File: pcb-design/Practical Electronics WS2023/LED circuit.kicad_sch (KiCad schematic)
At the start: 0 parts

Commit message: Update voltage regulator
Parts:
- added D10, D11, D12, D13, D14, D15, D16, D17, D3, D4, D5, D6, D7, D8, D9: WS2812B, LED_SMD:LED_WS2812B_PLCC4_5.0x5.0mm_P3.2mm, symbol LED:WS2812B
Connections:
- new net: D15.2 (DOUT), D16.4 (DIN)
- new net: D14.2 (DOUT), D15.4 (DIN)
- new net: D11.2 (DOUT), D12.4 (DIN)
- new net: D4.2 (DOUT), D5.4 (DIN)
- new net: D3.2 (DOUT), D4.4 (DIN)
- new net: D10.2 (DOUT), D11.4 (DIN)
- new net: D10.4 (DIN), D9.2 (DOUT)
- new net: D8.2 (DOUT), D9.4 (DIN)
- new net: D16.2 (DOUT), D17.4 (DIN)
- new net: D13.2 (DOUT), D14.4 (DIN)
- new net: D6.2 (DOUT), D7.4 (DIN)
- new net: D5.2 (DOUT), D6.4 (DIN)
- new net +5V: D10.1 (VDD), D11.1 (VDD), D12.1 (VDD), D13.1 (VDD), D14.1 (VDD), D15.1 (VDD), D16.1 (VDD), D17.1 (VDD), D3.1 (VDD), D4.1 (VDD), D5.1 (VDD), D6.1 (VDD), D7.1 (VDD), D8.1 (VDD), D9.1 (VDD)
- new net GND: D10.3 (VSS), D11.3 (VSS), D12.3 (VSS), D13.3 (VSS), D14.3 (VSS), D15.3 (VSS), D16.3 (VSS), D17.3 (VSS), D3.3 (VSS), D4.3 (VSS), D5.3 (VSS), D6.3 (VSS), D7.3 (VSS), D8.3 (VSS), D9.3 (VSS)
- new net LED_ON_BOARD: D3.4 (DIN)
- new net R1_DOUT: D7.2 (DOUT), D8.4 (DIN)
- new net R2_DOUT: D12.2 (DOUT), D13.4 (DIN)
- no-connect marks 0 -> 1
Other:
- note added: "Onboard LED matrix"

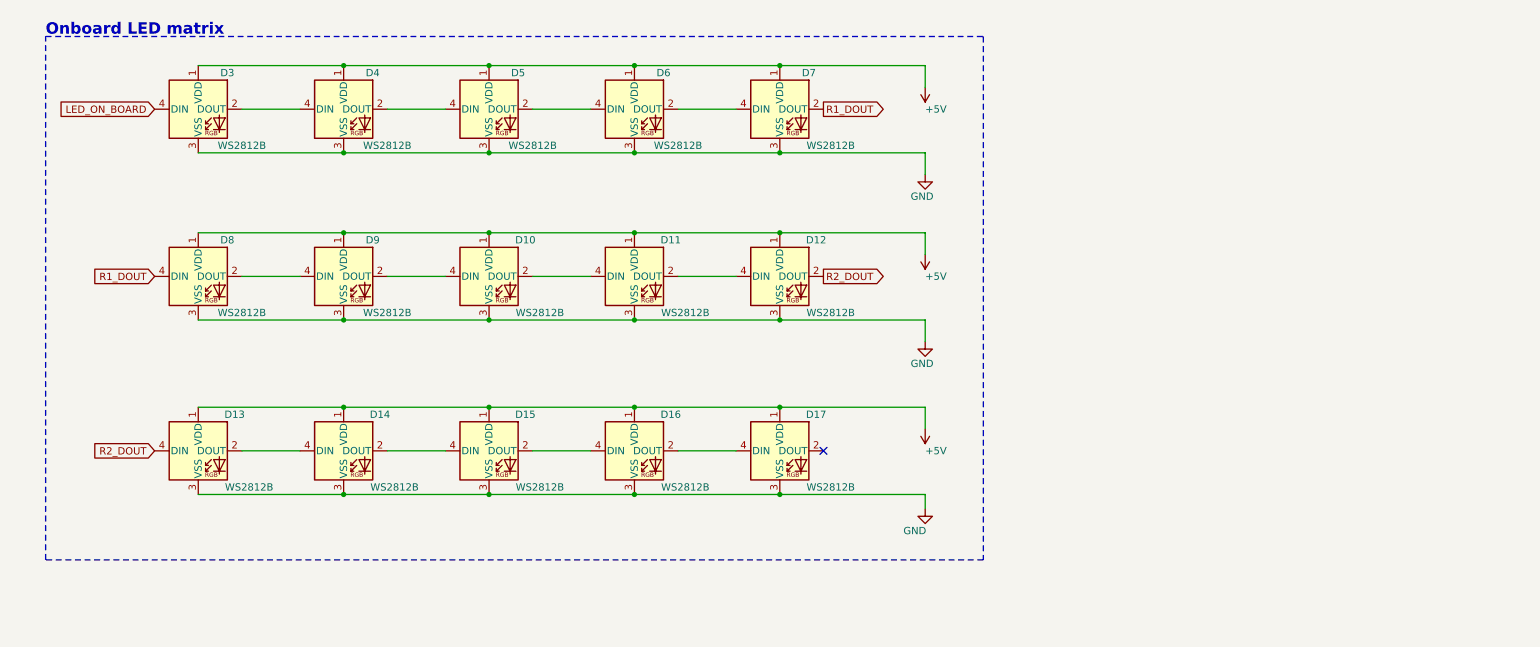
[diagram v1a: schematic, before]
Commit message: Power switch, logic switches, LED strip detection, onboard LEDs are 2x8.
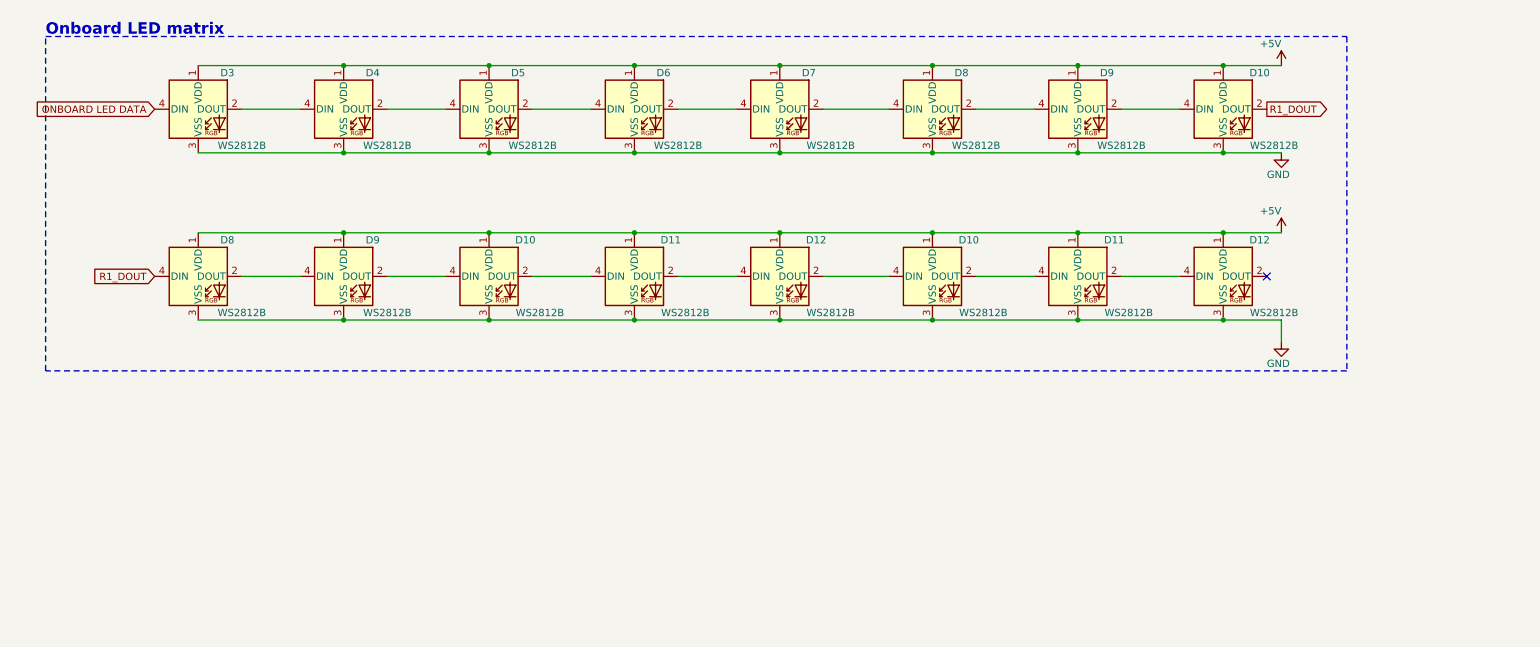
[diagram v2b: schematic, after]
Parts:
- removed D13, D14, D15, D16, D17: WS2812B, LED_SMD:LED_WS2812B_PLCC4_5.0x5.0mm_P3.2mm, symbol LED:WS2812B
- added D10 (x2), D11, D12, D8, D9: WS2812B, LED_SMD:LED_WS2812B_PLCC4_5.0x5.0mm_P3.2mm, symbol LED:WS2812B
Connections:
- net +5V: now also D10.1 (VDD), D10.1 (VDD), D11.1 (VDD), D12.1 (VDD), D8.1 (VDD), D9.1 (VDD)
- net GND: now also D10.3 (VSS), D10.3 (VSS), D11.3 (VSS), D12.3 (VSS), D8.3 (VSS), D9.3 (VSS)
- net R1_DOUT: now also D10.2 (DOUT); no longer D7.2 (DOUT)
- net LED_ON_BOARD renamed ONBOARD LED DATA
- net R2_DOUT: no longer names the net of D12.2 (DOUT)
- net R2_DOUT: now also D10.4 (DIN)
- new net: D8.2 (DOUT), D9.4 (DIN)
- new net: D7.2 (DOUT), D8.4 (DIN)
- new net: D10.4 (DIN), D9.2 (DOUT)
- new net: D11.2 (DOUT), D12.4 (DIN)
- new net: D10.2 (DOUT), D11.4 (DIN)

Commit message: Update schematic
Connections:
- net +5V renamed +12V

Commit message: Update schematic
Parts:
- removed D10 (x2), D11 (x2), D12 (x2): WS2812B, LED_SMD:LED_WS2812B_PLCC4_5.0x5.0mm_P3.2mm, symbol LED:WS2812B
- added C10, C11, C12, C13, C14, C15, C16, C17, C18, C19, C20, C21, C22, C23, C24, C25: 0.1uF, symbol Device:C
- added D10, D3, D4, D5, D6, D7: WS2812B, LED_SMD:LED_WS2812B_PLCC4_5.0x5.0mm_P3.2mm, symbol LED:WS2812B
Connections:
- net +12V: now also C10.1, C11.1, C12.1, C13.1, C14.1, C15.1, C16.1, C17.1, C18.1, C19.1, C20.1, C21.1, C22.1, C23.1, C24.1, C25.1, D10.1 (VDD), D3.1 (VDD), D4.1 (VDD), D5.1 (VDD), D6.1 (VDD), D7.1 (VDD)
- net GND: now also C10.2, C11.2, C12.2, C13.2, C14.2, C15.2, C16.2, C17.2, C18.2, C19.2, C20.2, C21.2, C22.2, C23.2, C24.2, C25.2, D10.3 (VSS), D3.3 (VSS), D4.3 (VSS), D5.3 (VSS), D6.3 (VSS), D7.3 (VSS)
- net R1_DOUT: now also D3.4 (DIN); no longer D8.4 (DIN)
- net at D9.2 (DOUT): now also D10.4 (DIN)
- new net: D7.2 (DOUT), D8.4 (DIN)
- new net: D5.2 (DOUT), D6.4 (DIN)
- new net: D4.2 (DOUT), D5.4 (DIN)
- new net: D6.2 (DOUT), D7.4 (DIN)
- new net: D3.2 (DOUT), D4.4 (DIN)
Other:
- moved on the sheet: D10, D3, D4, D5, D6, D7, D8, D9

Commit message: most of the footprints assigned
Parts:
- C10, C11, C12, C13, C14, C15, C16, C17, C18, C19, C20, C21, C22, C23, C24, C25: footprint (none) -> Capacitor_SMD:C_1206_3216Metric_Pad1.33x1.80mm_HandSolder
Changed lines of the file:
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@@
       (effects (font (size 1.27 1.27)) (justify left))
     )
-    (property "Footprint" "" (at 214.5792 33.274 0)
+    (property "Footprint" "Capacitor_SMD:C_1206_3216Metric_Pad1.33x1.80mm_HandSolder" (at 214.5792 33.274 0)
       (effects (font (size 1.27 1.27)) hide)
     )
@@
       (effects (font (size 1.27 1.27)) (justify left))
     )
-    (property "Footprint" "" (at 136.0932 33.274 0)
+    (property "Footprint" "Capacitor_SMD:C_1206_3216Metric_Pad1.33x1.80mm_HandSolder" (at 136.0932 33.274 0)
       (effects (font (size 1.27 1.27)) hide)
     )
@@
       (effects (font (size 1.27 1.27)) (justify left))
     )
-    (property "Footprint" "" (at 214.3252 86.106 0)
+    (property "Footprint" "Capacitor_SMD:C_1206_3216Metric_Pad1.33x1.80mm_HandSolder" (at 214.3252 86.106 0)
       (effects (font (size 1.27 1.27)) hide)
     )
@@
       (effects (font (size 1.27 1.27)) (justify left))
     )
-    (property "Footprint" "" (at 163.0172 86.106 0)
+    (property "Footprint" "Capacitor_SMD:C_1206_3216Metric_Pad1.33x1.80mm_HandSolder" (at 163.0172 86.106 0)
       (effects (font (size 1.27 1.27)) hide)
     )
@@
       (effects (font (size 1.27 1.27)) (justify left))
     )
-    (property "Footprint" "" (at 85.5472 33.274 0)
+    (property "Footprint" "Capacitor_SMD:C_1206_3216Metric_Pad1.33x1.80mm_HandSolder" (at 85.5472 33.274 0)
       (effects (font (size 1.27 1.27)) hide)
     )
@@
       (effects (font (size 1.27 1.27)) (justify left))
     )
-    (property "Footprint" "" (at 163.2712 33.274 0)
+    (property "Footprint" "Capacitor_SMD:C_1206_3216Metric_Pad1.33x1.80mm_HandSolder" (at 163.2712 33.274 0)
       (effects (font (size 1.27 1.27)) hide)
     )
@@
       (effects (font (size 1.27 1.27)) (justify left))
     )
-    (property "Footprint" "" (at 135.8392 86.106 0)
+    (property "Footprint" "Capacitor_SMD:C_1206_3216Metric_Pad1.33x1.80mm_HandSolder" (at 135.8392 86.106 0)
       (effects (font (size 1.27 1.27)) hide)
     )
@@
       (effects (font (size 1.27 1.27)) (justify left))
     )
-    (property "Footprint" "" (at 85.2932 86.106 0)
+    (property "Footprint" "Capacitor_SMD:C_1206_3216Metric_Pad1.33x1.80mm_HandSolder" (at 85.2932 86.106 0)
       (effects (font (size 1.27 1.27)) hide)
     )
@@
       (effects (font (size 1.27 1.27)) (justify left))
     )
-    (property "Footprint" "" (at 58.6232 33.274 0)
+    (property "Footprint" "Capacitor_SMD:C_1206_3216Metric_Pad1.33x1.80mm_HandSolder" (at 58.6232 33.274 0)
       (effects (font (size 1.27 1.27)) hide)
     )
@@
       (effects (font (size 1.27 1.27)) (justify left))
     )
-    (property "Footprint" "" (at 189.1792 86.106 0)
+    (property "Footprint" "Capacitor_SMD:C_1206_3216Metric_Pad1.33x1.80mm_HandSolder" (at 189.1792 86.106 0)
       (effects (font (size 1.27 1.27)) hide)
     )
@@
       (effects (font (size 1.27 1.27)) (justify left))
     )
-    (property "Footprint" "" (at 111.4552 86.106 0)
+    (property "Footprint" "Capacitor_SMD:C_1206_3216Metric_Pad1.33x1.80mm_HandSolder" (at 111.4552 86.106 0)
       (effects (font (size 1.27 1.27)) hide)
     )
@@
       (effects (font (size 1.27 1.27)) (justify left))
     )
-    (property "Footprint" "" (at 239.7252 86.106 0)
+    (property "Footprint" "Capacitor_SMD:C_1206_3216Metric_Pad1.33x1.80mm_HandSolder" (at 239.7252 86.106 0)
       (effects (font (size 1.27 1.27)) hide)
     )
@@
       (effects (font (size 1.27 1.27)) (justify left))
     )
-    (property "Footprint" "" (at 189.1792 33.274 0)
+    (property "Footprint" "Capacitor_SMD:C_1206_3216Metric_Pad1.33x1.80mm_HandSolder" (at 189.1792 33.274 0)
       (effects (font (size 1.27 1.27)) hide)
     )
@@
       (effects (font (size 1.27 1.27)) (justify left))
     )
-    (property "Footprint" "" (at 239.9792 33.274 0)
+    (property "Footprint" "Capacitor_SMD:C_1206_3216Metric_Pad1.33x1.80mm_HandSolder" (at 239.9792 33.274 0)
       (effects (font (size 1.27 1.27)) hide)
     )
@@
       (effects (font (size 1.27 1.27)) (justify left))
     )
-    (property "Footprint" "" (at 58.3692 86.106 0)
+    (property "Footprint" "Capacitor_SMD:C_1206_3216Metric_Pad1.33x1.80mm_HandSolder" (at 58.3692 86.106 0)
       (effects (font (size 1.27 1.27)) hide)
     )
@@
       (effects (font (size 1.27 1.27)) (justify left))
     )
-    (property "Footprint" "" (at 111.7092 33.274 0)
-      (effects (font (size 1.27 1.27)) hide)
-    )
+    (property "Footprint" "Capacitor_SMD:C_1206_3216Metric_Pad1.33x1.80mm_HandSolder" (at 111.7092 33.274 0)
+      (effects (font (size 1.27 1.27)) hide)
+    )
